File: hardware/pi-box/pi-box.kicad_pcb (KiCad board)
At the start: 2 copper layers, 65 x 56 mm, 11 parts, among them J1 Raspberry_Pi_4, J2 RJ45, J3 RJ45

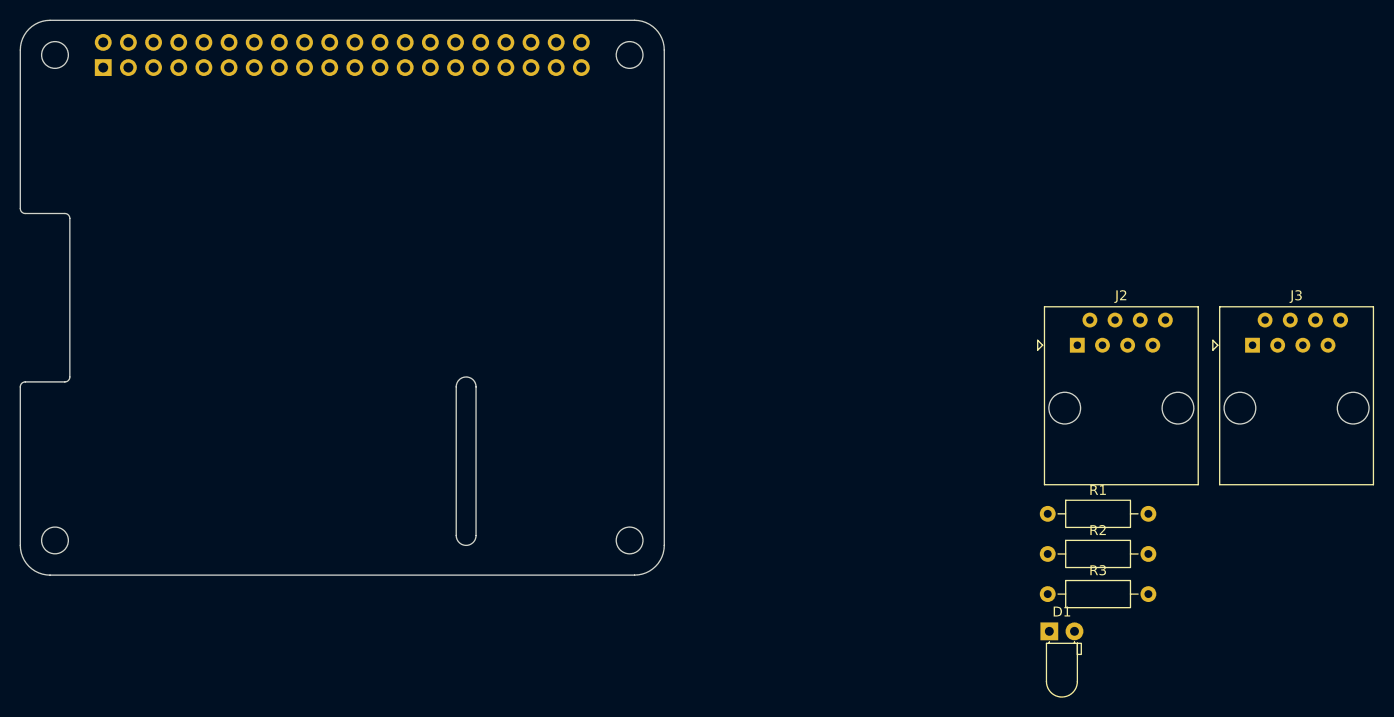
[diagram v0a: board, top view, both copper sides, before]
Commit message: Place pi-box components
Jacks on the short edge facing the same way as the Pi's own ports, 18 mm
apart and sharing an X so the cables leave in a line. LED beside them, since
a status light you have to pull a panel to read is one you will never look
at. Resistors in a column near the header, where their nets already are.

No overhang, because the DAC HAT is off the table: it uses the whole HAT
footprint, no stacking header sold gives more than about 8.5 mm of pin above
the board against the 13.5 mm these jacks need, and with the HAT the audio
cables leave in the wrong direction anyway. The USB DAC already works and can
sit wherever it likes. That also means a plain 2x20 socket is enough, though
the footprint takes either.

DRC finds three violations, all the same cause: the HAT's display-ribbon slot
at X 68-70 passes 0.11 mm from J3's SDA pad against a 0.5 mm rule. Deleting
the slot next, since nothing on this rig will ever use the camera or display
connectors.

Co-Authored-By: Claude Opus 5 <noreply@anthropic.com>
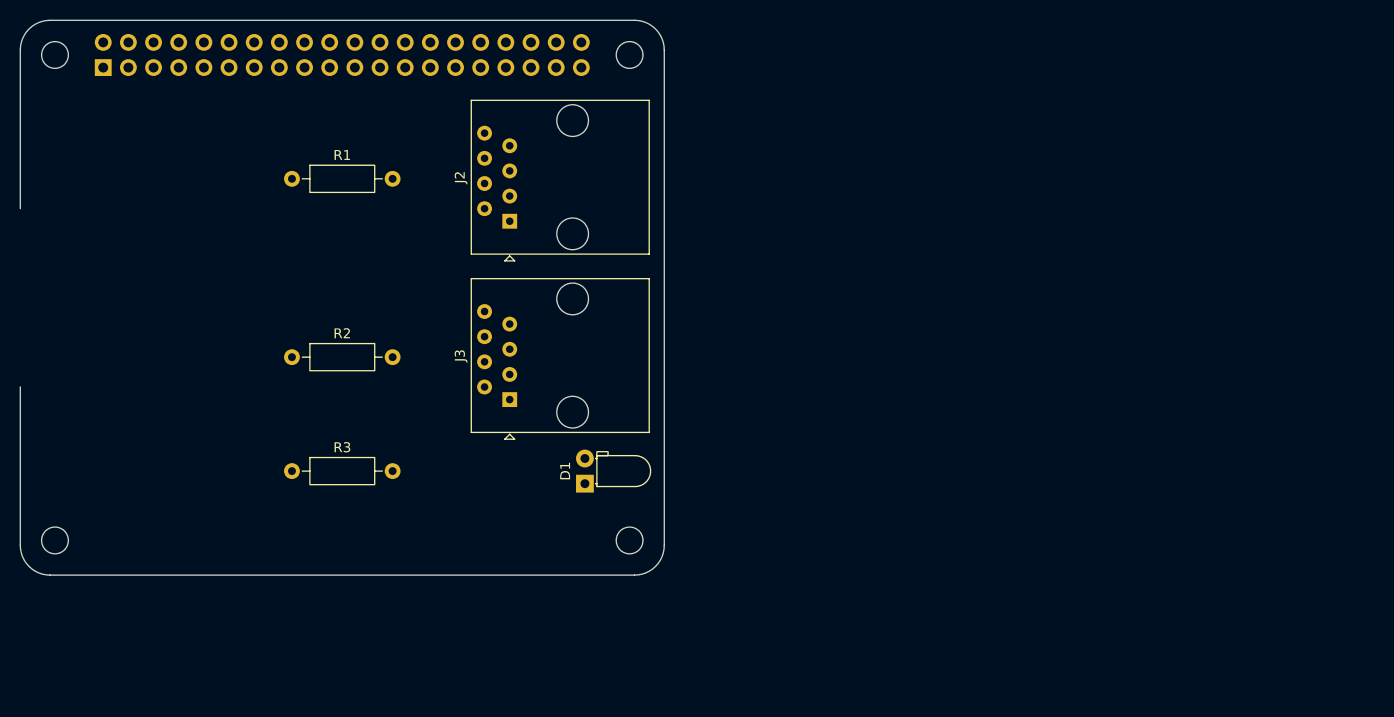
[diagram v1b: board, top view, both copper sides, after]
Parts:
- moved R1 83.4 mm to (51.4, 62.0)
- moved R2 78.8 mm to (51.4, 80.0)
- moved R3 77.3 mm to (51.4, 91.5)
- moved J3 75.2 mm to (73.4, 84.3), turned to 90 degrees
- moved J2 58.6 mm to (73.4, 66.3), turned to 90 degrees
- moved D1 49.2 mm to (81.0, 92.8), turned to 90 degrees
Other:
- outline, holes or cut-outs redrawn
- board text removed: "CAMERA (OPTIONAL)"
- board text removed: "DISPLAY (OPTIONAL)"
- board text removed: "Extend PCB edge 0.5mm if using SMT header"

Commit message: Close the pi-box outline: DRC clean before routing
Deletes the HAT's camera and display ribbon cutouts, which nothing on this
rig will ever use, and closes the left edge as a single straight segment. The
display slot was the reason DRC failed: it passed 0.11 mm from J3's SDA pad
against a 0.5 mm rule, a gap invisible at any sane zoom and one a fab house
would have resolved by routing through the pad.

Removing them opened the perimeter, since the left-edge notch was the
perimeter along that stretch rather than a hole in it. The replacement
segment initially landed on F.Cu instead of Edge.Cuts — drawn with the
routing tool rather than the graphics tool — which reads as a copper trace
sitting on the board boundary and leaves the outline still open. Worth
recording because the two tools look alike and the symptom does not point at
the cause.

Now 0 DRC violations, 0 footprint errors, outline closed with no dangling
endpoints. The 31 unconnected pads are the routing, which is next.

Co-Authored-By: Claude Opus 5 <noreply@anthropic.com>
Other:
- outline, holes or cut-outs redrawn
- board text removed: "PoE"
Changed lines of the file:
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@@
 			(at -1.27 -51.03 90)
 			(layer "B.Fab")
+			(hide yes)
 			(effects
 				(font
@@
 	)
 	(gr_line
-		(start 24 49)
-		(end 24 48.5)
-		(stroke
-			(width 0.1)
-			(type solid)
-		)
-		(layer "Dwgs.User")
-	)
-	(gr_line
-		(start 24 65)
-		(end 24 83)
-		(stroke
-			(width 0.1)
-			(type solid)
-		)
-		(layer "Dwgs.User")
-	)
-	(gr_line
 		(start 89 49)
 		(end 89 48.5)
@@
 	(gr_line
 		(start 24 49)
-		(end 24 65)
-		(stroke
-			(width 0.1)
-			(type solid)
+		(end 24 99)
+		(stroke
+			(width 0.05)
+			(type default)
 		)
 		(layer "Edge.Cuts")
@@
 		(layer "Edge.Cuts")
 	)
-	(gr_line
-		(start 24 83)
-		(end 24 99)
-		(stroke
-			(width 0.1)
-			(type solid)
-		)
-		(layer "Edge.Cuts")
-	)
 	(gr_arc
 		(start 27 102)
@@
 		)
 		(layer "Edge.Cuts")
-	)
-	(gr_text "PoE"
-		(at 85.5 55.64 0)
-		(layer "Dwgs.User")
-		(effects
-			(font
-				(size 1 1)
-				(thickness 0.15)
-			)
-		)
 	)
 	(gr_text "RJ45"
@@
 			)
 		)
-	)
-	(zone
-		(layer "B.Cu")
-		(name "PoE")
-		(hatch full 0.508)
-		(connect_pads
-			(clearance 0)
-		)
-		(min_thickness 0.254)
-		(keepout
-			(tracks allowed)
-			(vias allowed)
-			(pads allowed)
-			(copperpour allowed)
-			(footprints not_allowed)
-		)
-		(placement
-			(enabled no)
-			(sheetname "")
-		)
-		(fill
-			(thermal_gap 0.508)
-			(thermal_bridge_width 0.508)
-			(island_removal_mode 0)
-		)
-		(polygon
-			(pts
-				(xy 88 58.14) (xy 83 58.14) (xy 83 53.14) (xy 88 53.14)
-			)
-		)

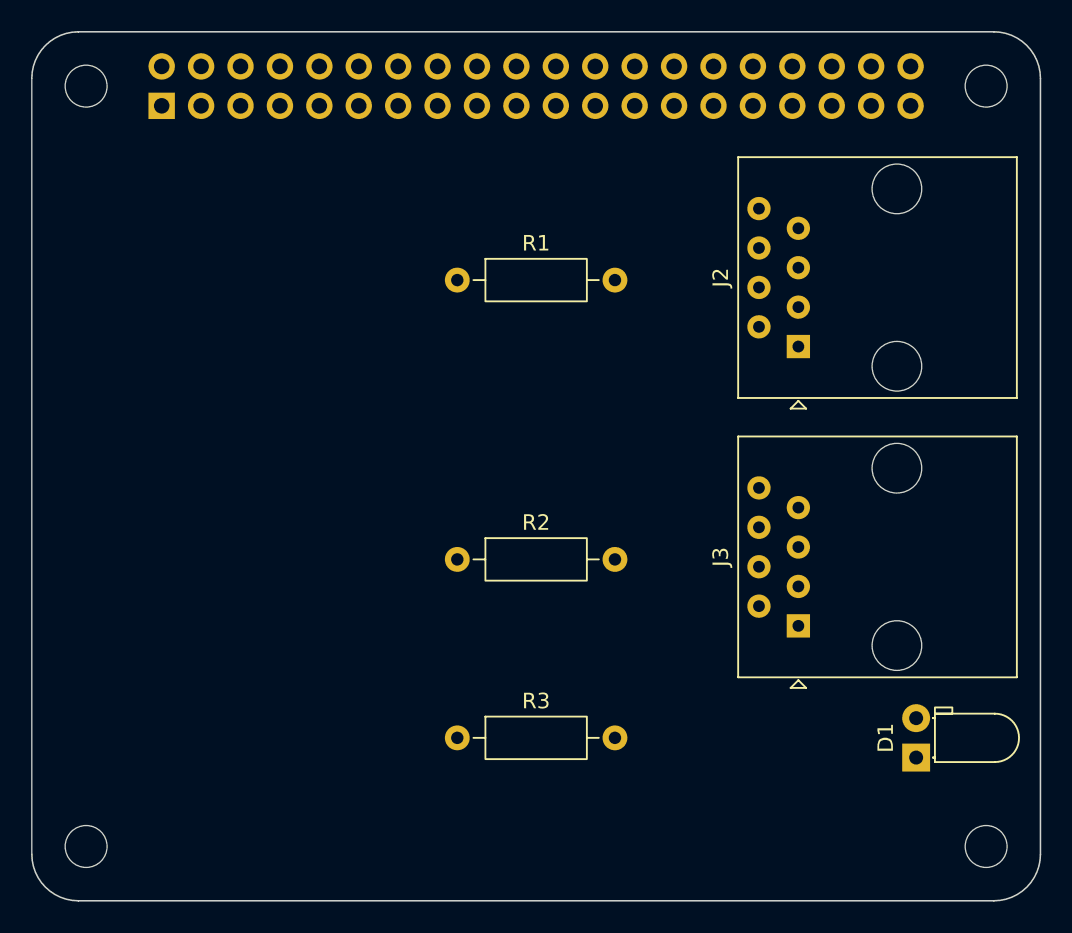
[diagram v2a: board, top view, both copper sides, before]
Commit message: Route pi-box: DRC clean, no vias, unbroken ground plane
All seven signal nets on F.Cu with zero vias, so the GND zone on B.Cu is a
single continuous sheet rather than something with slots cut through it. That
was not really planned — it fell out of placing parts so their nets did not
need to cross — but it is the best case for a two-layer board and worth not
undoing during fine-tuning.

The ground zone connects 17 pads that would otherwise have been 17 hand-drawn
tracks. Its thermal relief clearance had to come down from 0.5 mm to 0.2 mm:
at 0.5 the copper could not fit between the header's pads, which sit on a
2.54 mm pitch with about 0.84 mm between pad edges, so five interior GND pads
were stranded while the ones on the outside connected fine.

Two things cost time and are worth recording. A zone fill is stored in the
file, so moving parts after filling leaves copper sitting exactly where the
pads now are — that produced 40 violations that all evaporated on a refill,
and there is no visual cue that a fill is stale. And +3.3V reaches the header
at both pin 1 and pin 17, which are the same net and are joined on the Pi
itself, so the board looked finished while its own 3.3V rail was in two
pieces. Joined on-board rather than relying on what it plugs into.

Placement still to fine-tune.

Co-Authored-By: Claude Opus 5 <noreply@anthropic.com>
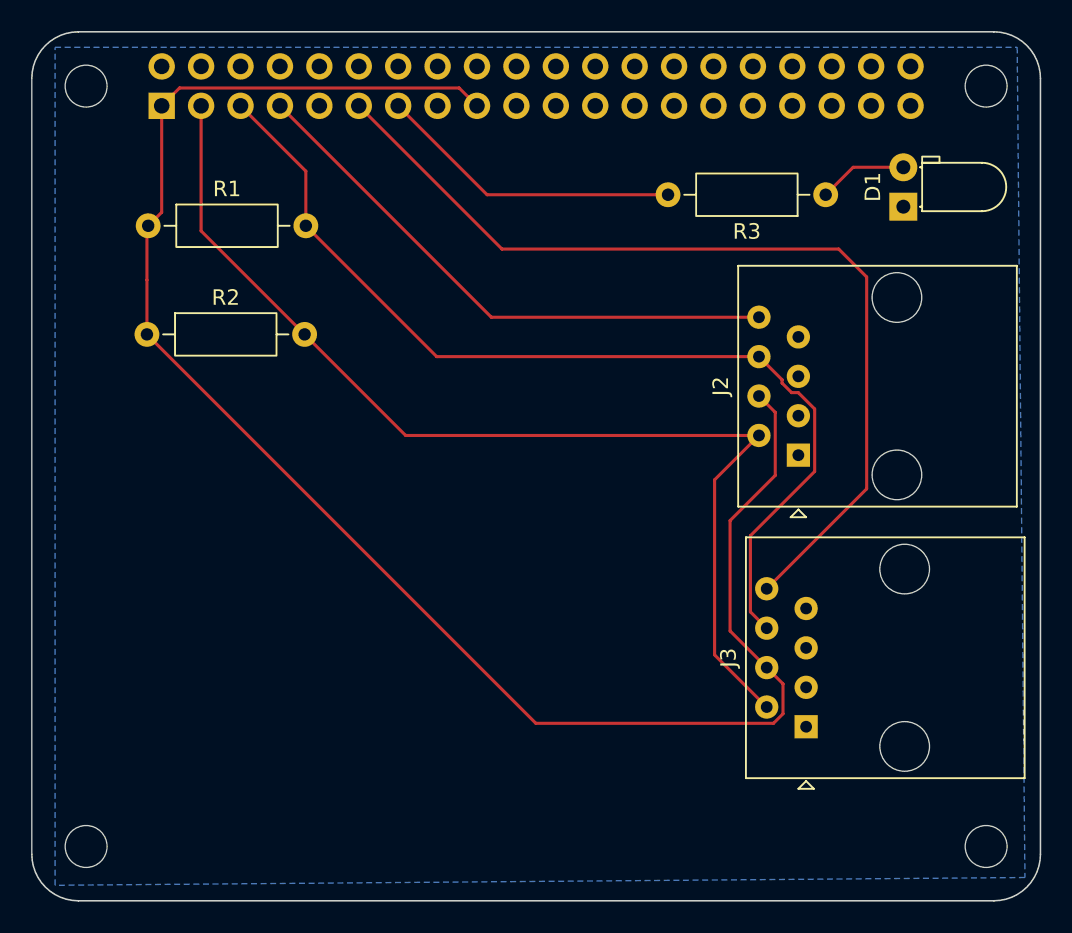
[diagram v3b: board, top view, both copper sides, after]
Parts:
- moved R3 42.3 mm to (75.2, 56.5), turned to 180 degrees
- moved D1 35.5 mm to (80.2, 57.3)
- moved R2 24.7 mm to (31.4, 65.5)
- moved R1 20.2 mm to (31.5, 58.5)
- moved J2 7.00 mm to (73.4, 73.3)
- moved J3 6.52 mm to (73.9, 90.8)
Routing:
- net +3.3V: track 0.00 -> 111.5 mm
- net /SDA: track 0.00 -> 69.5 mm
- net /SCL: track 0.00 -> 63.6 mm
- net /INT_REAR: track 0.00 -> 60.1 mm
- net /INT_FRONT: track 0.00 -> 36.5 mm
- net Net-(J1-GPIO27/SDIO_DAT3): track 0.00 -> 19.8 mm
- net Net-(D1-A): track 0.00 -> 5.74 mm
- added copper zone on B.Cu, net GND
